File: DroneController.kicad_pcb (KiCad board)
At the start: 2 copper layers, 0.6 x 6.4 mm, 37 parts, among them P1 USB_C_Plug, U1 TP74333PDQNR, U2 TPS62152RGTR, U3 BMP280, U4 MPU-6500, U6 L86-M33, X1 X50328MSB2GI

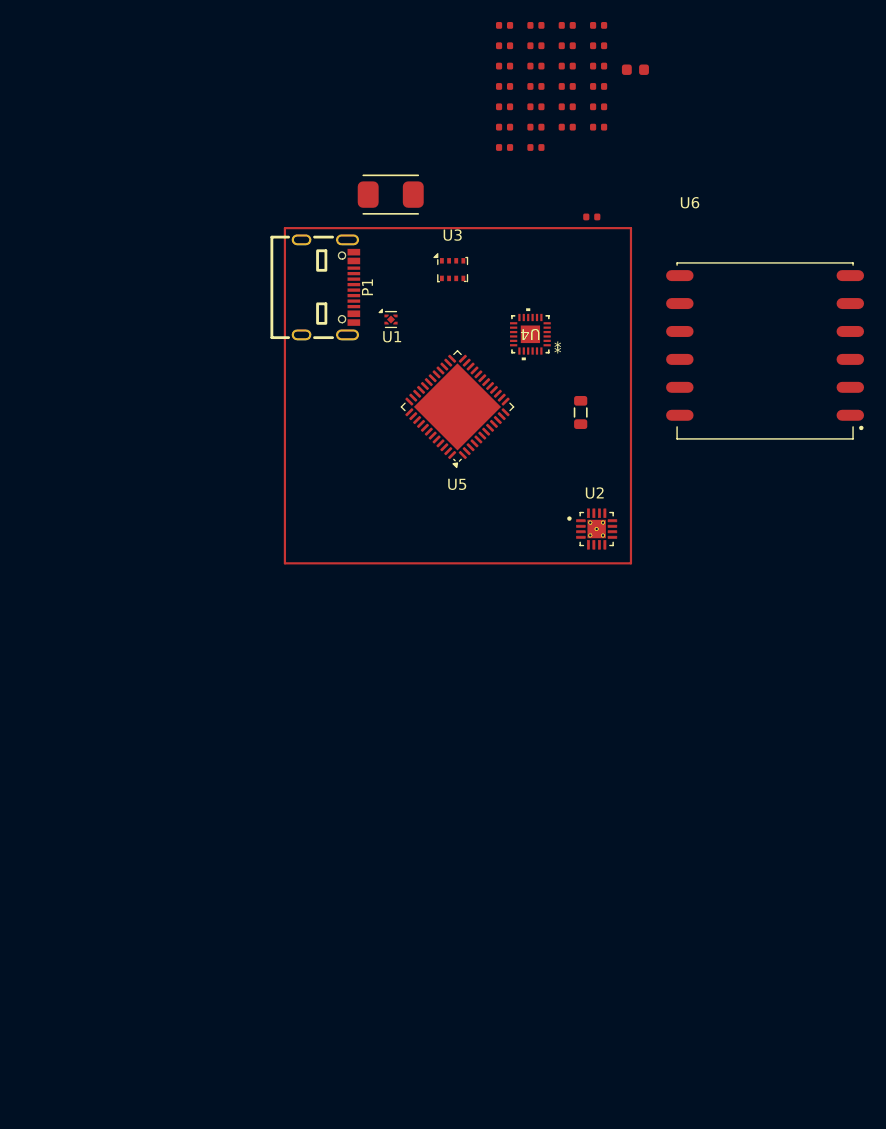
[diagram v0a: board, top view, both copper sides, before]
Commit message: Updated STM32 and overhauled SPI wiring, added external flash memory, added LoRa Transciever, moved buck converter to ESC-Board which will handle power distrubution, signficant progress on PCB design.
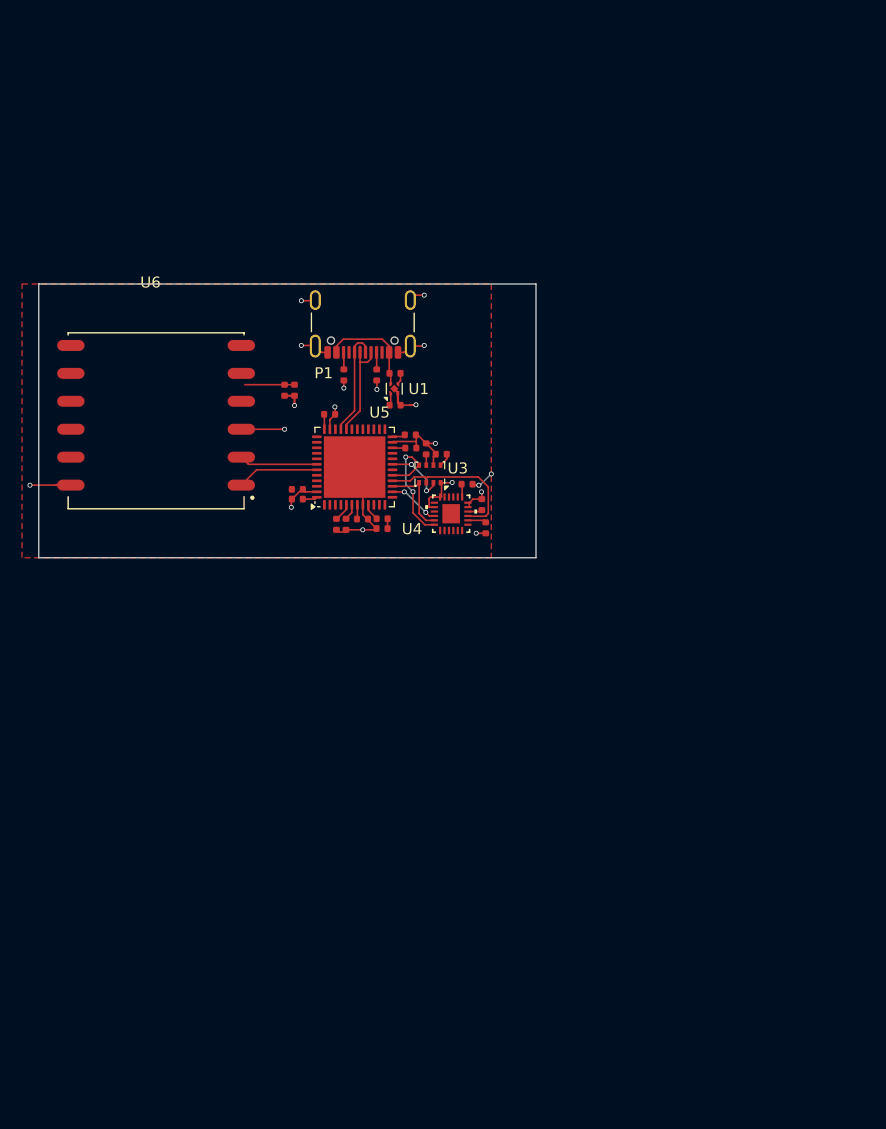
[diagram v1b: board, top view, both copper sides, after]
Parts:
- removed C11: 10uF, PCM_JLCPCB:C_0603
- removed C13: 3.3nF, PCM_JLCPCB:C_0402
- removed C19, C22, C23, C24, C8: 100nF, PCM_JLCPCB:C_0402
- removed L1: 2.2uH,50mA, PCM_JLCPCB:L_0805
- removed R3: 100kΩ, PCM_JLCPCB:R_0402
- removed U2: TPS62152RGTR, TPS62152RGTR:QFN50P300X300X100-17N
- removed X1: X50328MSB2GI, PCM_JLCPCB:CRYSTAL-SMD_L5.0-W3.2
- added C17: 100nF, PCM_JLCPCB:C_0402, F.Cu at (128.7, 101.4)
- C12: value 1uF -> 100nF
- P1: footprint MC311D:USB-C-SMD_MC-311D -> USB-C:USB-C
- moved U6 55.7 mm to (104.1, 98.3), turned to 180 degrees
- moved C10 48.9 mm to (120.5, 108.2), turned to 90 degrees
- moved C27 48.1 mm to (122.9, 107.7)
- moved C20 46.2 mm to (124.7, 107.7)
- moved C1 45.7 mm to (134.1, 108.5), turned to 90 degrees
- moved C21 45.3 mm to (124.7, 108.6), turned to 180 degrees
- moved C26 42.1 mm to (127.3, 101.3)
- moved C2 41.8 mm to (133.8, 106.4), turned to -90 degrees
- moved C7 40.6 mm to (121.4, 108.2), turned to -90 degrees
- moved C31 40.4 mm to (116.7, 96.0), turned to -90 degrees
- moved C18 38.6 mm to (117.0, 105.9), turned to 180 degrees
- moved C3 38.2 mm to (132.4, 104.6), turned to 180 degrees
- moved C12 38.1 mm to (130.1, 101.8), turned to 180 degrees
- moved C25 36.5 mm to (117.0, 105.0), turned to 180 degrees
- moved C15 34.4 mm to (115.8, 96.0), turned to -90 degrees
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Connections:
- C10 pad 1: Net-(C10-Pad1) -> GND
- C12 pad 1: Net-(C12-Pad1) -> +3.3V
- C14 pad 2: unconnected-(C14-Pad2) -> GND
- C18 pad 1: VDD -> +3.3V
- C25 pad 2: VDD -> +3.3V
- C4 pad 2: VDD -> +3.3V
- C7 pad 2: Net-(C7-Pad2) -> GND
- C9 pad 2: VDD -> +3.3V
- P1 pad B6: /USB_FS_DM -> /USB_FS_DP
- P1 pad B7: /USB_FS_DP -> /USB_FS_DM
- U3 pad 2: /SPI2_NSS -> /SPI5_NSS
- U3 pad 3: /SPI2_MOSI -> /SPI1_MISO
- U3 pad 4: /SPI2_SCK -> /SPI1_SCK
- U3 pad 5: /SPI2_MISO -> /SPI1_MOSI
- U4 pad 11: unconnected-(U4-FSYNC-Pad11) -> GND
- U4 pad 12: unconnected-(U4-INT-Pad12) -> GND
- U5 pad 1: +3.3V -> +BATT
- U5 pad 19: unconnected-(U5-PB1-Pad19) -> /SPI5_NSS
- U5 pad 24: VDD -> +3.3V
- U5 pad 25: /SPI2_NSS -> unconnected-(U5-PB12-Pad25)
- U5 pad 26: /SPI2_SCK -> unconnected-(U5-PB13-Pad26)
- U5 pad 27: /SPI2_MISO -> unconnected-(U5-PB14-Pad27)
- U5 pad 28: /SPI2_MOSI -> unconnected-(U5-PB15-Pad28)
- U5 pad 36: VDD -> +3.3V
- U5 pad 48: VDD -> +3.3V
- U5 pad 49: unconnected-(U5-PAD-Pad49) -> GND
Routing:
- net GND: track 0.00 -> 56.0 mm, vias 0 -> 17
- net /SPI1_MISO: track 0.00 -> 14.0 mm
- net /SPI1_MOSI: track 0.00 -> 12.2 mm, vias 0 -> 2
- net +3.3V: track 0.00 -> 11.3 mm, vias 0 -> 2
- net /USB_FS_DP: track 0.00 -> 9.88 mm
- net +5V: track 0.00 -> 9.35 mm
- net /USB_FS_DM: track 0.00 -> 9.21 mm
- net /USART1_RX: track 0.00 -> 7.44 mm
- net /USART1_TX: track 0.00 -> 7.13 mm
- net /SPI1_SCK: track 0.00 -> 7.13 mm
- net /SPI5_NSS: track 0.00 -> 5.76 mm, vias 0 -> 2
- net /SPI1_NSS: track 0.00 -> 4.62 mm, vias 0 -> 2
- net +BATT: track 0.00 -> 4.18 mm
- net Net-(U5-PH0-OSC_IN): track 0.00 -> 1.83 mm
- net Net-(U5-PH1-OSC_OUT): track 0.00 -> 1.67 mm
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- added copper zone on F.Cu, net +3.3V
- added copper zone on In1.Cu, net GND
- added copper zone on In2.Cu, net GND
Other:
- board size 0.6 x 6.4 mm -> 45.2 x 24.9 mm
- copper layers 2 -> 4

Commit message: Finalized PCB Design
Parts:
- removed C14, C16: 1uF, PCM_JLCPCB:C_0402
- removed C4: 4.7uF, PCM_JLCPCB:C_0402
- removed U1: TP74333PDQNR, Package_DFN_QFN:OnSemi_XDFN4-1EP_1.0x1.0mm_EP0.52x0.52mm
- added AE1: 915MHZ Antenna, Connector_Coaxial:SMA_BAT_Wireless_BWSMA-KWE-Z001, F.Cu at (147.6, 122.6)
- added C28: 100nF, PCM_JLCPCB:C_0402, F.Cu at (143.9, 115.1)
- added C29: 100nF, PCM_JLCPCB:C_0402, F.Cu at (122.0, 132.2)
- added C5: 10uF, PCM_JLCPCB:C_0402, F.Cu at (142.6, 115.1)
- added C6: 10uF, PCM_JLCPCB:C_0402, F.Cu at (107.5, 115.0)
- added C8: 10uF, PCM_JLCPCB:C_0402, F.Cu at (104.0, 115.0)
- added J1: Connector, TerminalBlock:TerminalBlock_MaiXu_MX126-5.0-02P_1x02_P5.00mm, F.Cu at (145.5, 147.1)
- added J2: Connector, TerminalBlock:TerminalBlock_MaiXu_MX126-5.0-02P_1x02_P5.00mm, F.Cu at (145.5, 135.4)
- added J3: Connector, TerminalBlock:TerminalBlock_MaiXu_MX126-5.0-02P_1x02_P5.00mm, F.Cu at (137.6, 156.0)
- added R3: 5.1kΩ, PCM_JLCPCB:R_0402, F.Cu at (137.7, 126.8)
- added R4: 5.1kΩ, PCM_JLCPCB:R_0402, F.Cu at (127.2, 128.1)
- added R5: 5.1kΩ, PCM_JLCPCB:R_0402, F.Cu at (111.1, 115.5)
- added SW1: SW_SPDT, Switches:SW-SMD_MSK12CO2, F.Cu at (135.9, 139.9)
- added U2: W25Q16JVSS, Package_SO:SOIC-8_5.3x5.3mm_P1.27mm, F.Cu at (132.5, 127.0)
- added U7: 915MHz, Lora1276:COMM-SMD_LORA1276-C1-915MHZ, F.Cu at (132.6, 115.6)
- added U9: AP7361C-33E, Package_TO_SOT_SMD:SOT-223-3_TabPin2, F.Cu at (105.9, 110.0)
- moved U6 52.3 mm to (116.5, 149.1), turned to -90 degrees
- moved P1 43.4 mm to (104.1, 128.0), turned to -90 degrees
- moved C15 41.5 mm to (113.1, 137.4), turned to 0 degrees
- moved C31 40.7 mm to (113.1, 136.5), turned to 0 degrees
- moved R2 36.9 mm to (109.8, 129.7), turned to 180 degrees
- moved C12 36.3 mm to (114.9, 134.9), turned to -90 degrees
- moved C17 36.1 mm to (116.7, 135.4), turned to 180 degrees
- moved R1 35.2 mm to (109.8, 126.8), turned to 180 degrees
- moved U3 32.3 mm to (117.0, 133.6), turned to 0 degrees
- moved C25 25.1 mm to (114.6, 130.0), turned to -90 degrees
- moved C9 24.8 mm to (116.5, 122.4), turned to -90 degrees
- moved U5 24.7 mm to (119.3, 127.5), turned to 180 degrees
- moved C3 24.5 mm to (111.9, 118.0), turned to 90 degrees
- moved C18 24.3 mm to (113.4, 130.0), turned to 90 degrees
- moved C26 23.3 mm to (117.7, 122.4), turned to 90 degrees
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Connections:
- U3 pad 2: /SPI5_NSS -> /SPI3_NSS
- U3 pad 3: /SPI1_MISO -> /SPI3_MISO
- U3 pad 4: /SPI1_SCK -> /SPI3_SCK
- U3 pad 5: /SPI1_MOSI -> /SPI3_MOSI
- U4 pad 22: /SPI1_NSS -> /SPI2_NSS
- U4 pad 23: /SPI1_SCK -> /SPI2_SCK
- U4 pad 24: /SPI1_MOSI -> /SPI2_MOSI
- U4 pad 25: unconnected-(U4-Pad25) -> GND
- U4 pad 9: /SPI1_MISO -> /SPI2_MISO
- U5 pad 12: unconnected-(U5-PA2-Pad12) -> /USART2_TX
- U5 pad 13: unconnected-(U5-PA3-Pad13) -> /USART2_RX
- U5 pad 18: unconnected-(U5-PB0-Pad18) -> /SPI5_SCK
- U5 pad 20: unconnected-(U5-PB2-Pad20) -> /Lora_RES
- U5 pad 25: unconnected-(U5-PB12-Pad25) -> /SPI2_NSS
- U5 pad 26: unconnected-(U5-PB13-Pad26) -> /SPI2_SCK
- U5 pad 27: unconnected-(U5-PB14-Pad27) -> /SPI2_MISO
- U5 pad 28: unconnected-(U5-PB15-Pad28) -> /SPI2_MOSI
- U5 pad 38: unconnected-(U5-PA15-Pad38) -> /SPI3_NSS
- U5 pad 39: unconnected-(U5-PB3-Pad39) -> /SPI3_SCK
- U5 pad 40: unconnected-(U5-PB4-Pad40) -> /SPI3_MISO
- U5 pad 41: unconnected-(U5-PB5-Pad41) -> /SPI3_MOSI
- U5 pad 44: unconnected-(U5-BOOT0-Pad44) -> Net-(SW1-B)
- U6 pad 6: unconnected-(U6-1PPS-Pad6) -> GND
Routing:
- net +3.3V: track 11.3 -> 71.6 mm, vias 2 -> 10
- net GND: track 56.0 -> 106.7 mm, vias 17 -> 57
- net /USART2_TX: track 0.00 -> 44.2 mm, vias 0 -> 2
- net /USART2_RX: track 0.00 -> 43.0 mm, vias 0 -> 2
- net +BATT: track 4.18 -> 45.2 mm, vias 0 -> 2
- net /SPI1_MOSI: track 12.2 -> 37.7 mm
- net Net-(SW1-B): track 0.00 -> 21.6 mm
- net /SPI1_SCK: track 7.13 -> 26.6 mm
- net /SPI1_MISO: track 14.0 -> 32.0 mm
- net /SPI2_MISO: track 0.00 -> 17.0 mm
- net /SPI5_NSS: track 5.76 -> 20.6 mm
- net +5V: track 9.35 -> 21.6 mm
- net /Lora_RES: track 0.00 -> 9.73 mm, vias 0 -> 2
- net /SPI2_NSS: track 0.00 -> 7.84 mm, vias 0 -> 2
- net /SPI2_MOSI: track 0.00 -> 7.67 mm, vias 0 -> 2
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- added copper zone on F.Cu, net GND
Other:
- board size 45.2 x 24.9 mm -> 50.7 x 56.1 mm
- board text added: "Flight Controller"
- board text added: "J3"

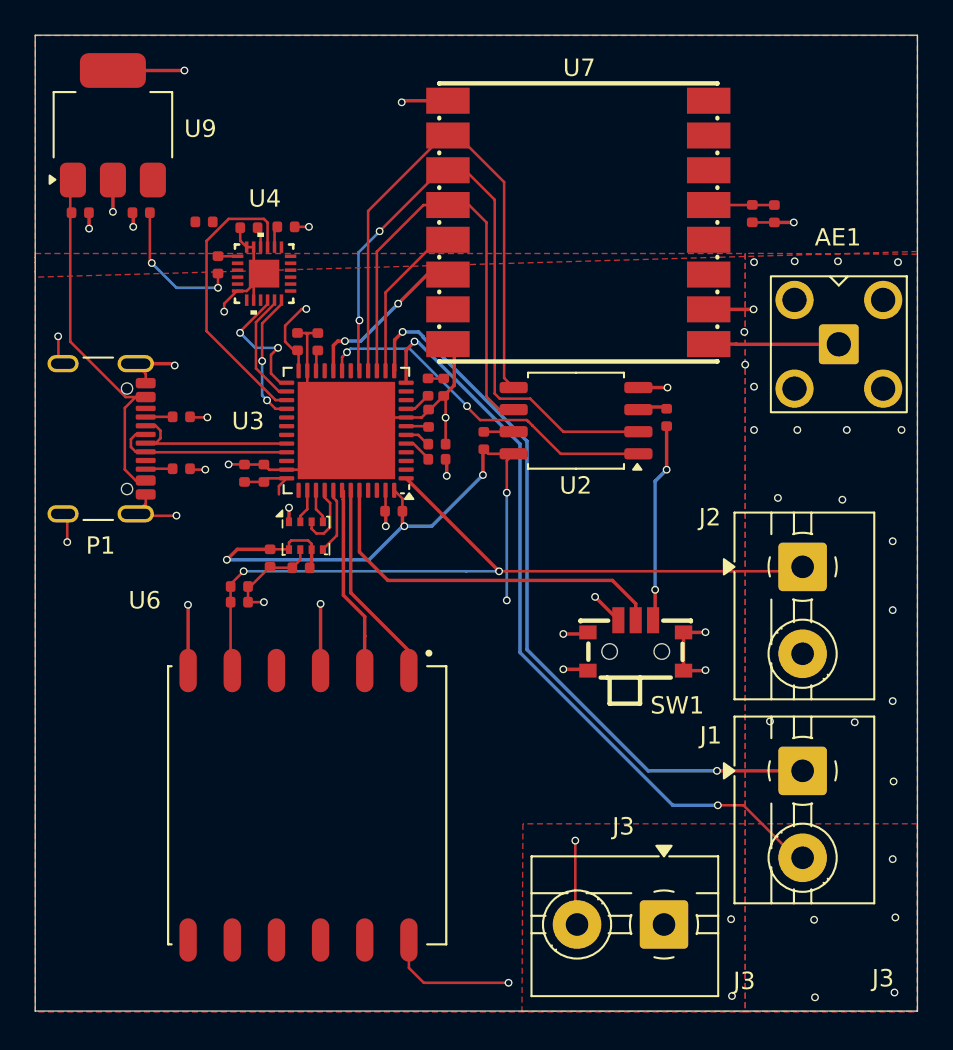
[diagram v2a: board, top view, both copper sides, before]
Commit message: Added 3D Models, Changes to Copper Zone, Added Crystal Oscillator to PCB.
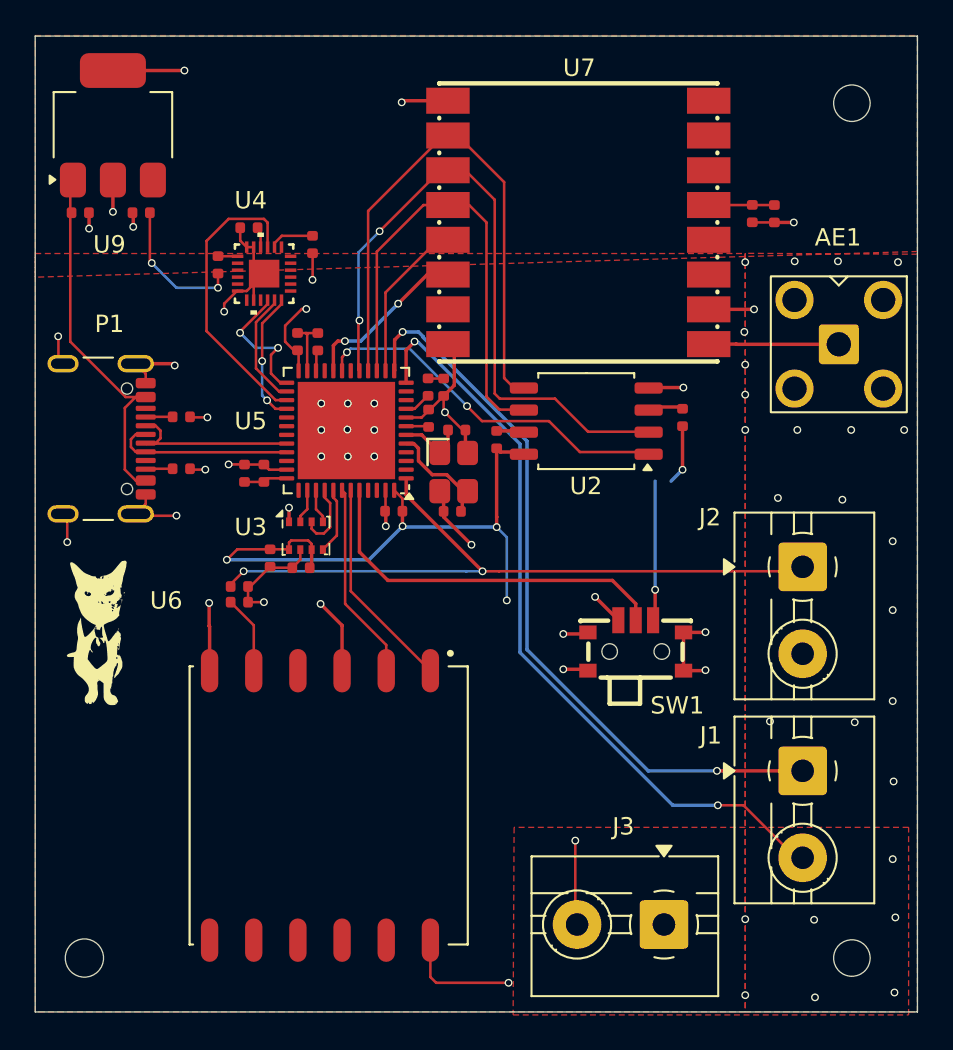
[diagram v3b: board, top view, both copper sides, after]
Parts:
- removed R5: 5.1kΩ, PCM_JLCPCB:R_0402
- added G***: LOGO, LOGO, F.Cu at (104.9, 139.2)
- added REF**: MountingHole_2.2mm_M2, MountingHole:MountingHole_2.2mm_M2, F.Cu at (104.2, 157.9)
- added REF**: MountingHole_2.1mm, MountingHole:MountingHole_2.1mm, F.Cu at (148.4, 108.7)
- added REF**: MountingHole_2.1mm, MountingHole:MountingHole_2.1mm, F.Cu at (148.4, 157.9)
- added X1: X322512MSB4SI, PCM_JLCPCB:CRYSTAL-SMD_4P-L3.2-W2.5-BL, F.Cu at (125.5, 129.9)
- moved C10 3.12 mm to (125.4, 132.2), turned to 0 degrees
- moved C1 1.83 mm to (117.3, 116.8), turned to 90 degrees
- moved C7 1.40 mm to (125.6, 127.5)
- moved U6 1.24 mm to (117.8, 149.1)
- moved R3 0.91 mm to (138.6, 126.8)
- moved R4 0.74 mm to (127.9, 128.1)
- moved U2 0.59 mm to (133.1, 127.0)
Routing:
- net GND: track 106.7 -> 98.7 mm, vias 57 -> 66
- net Net-(U5-PH0-OSC_IN): track 1.83 -> 6.41 mm
- net Net-(U5-PH1-OSC_OUT): track 1.67 -> 3.88 mm
- net +3.3V: track 71.6 -> 70.0 mm, vias 10 -> 9
- net /SPI5_NSS: track 20.6 -> 21.1 mm
- net /USART1_RX: track 11.8 -> 12.3 mm
- net /USART1_TX: track 10.9 -> 11.4 mm
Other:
- board text added: "U4"
- board text added: "U5"
- board text removed: "J3"

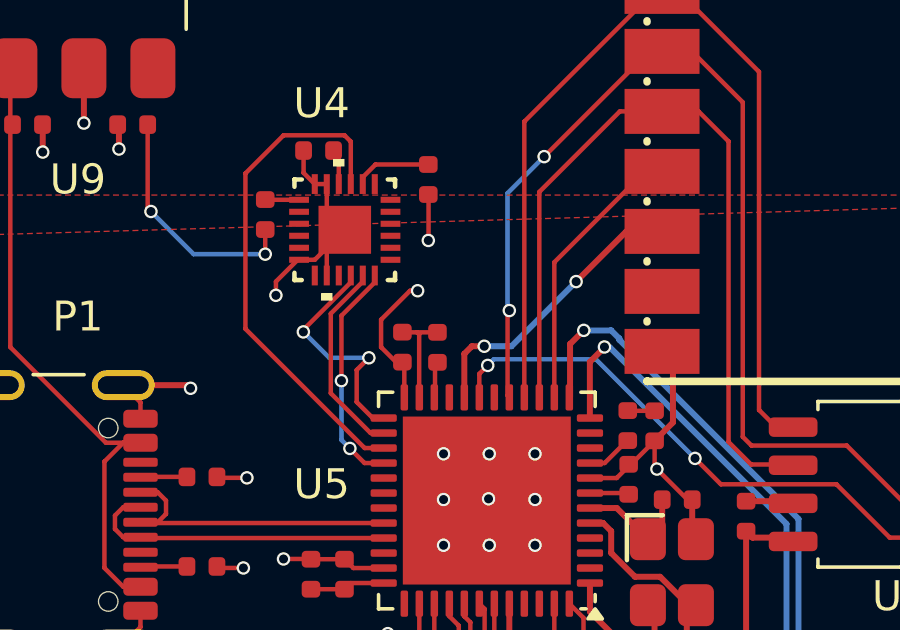
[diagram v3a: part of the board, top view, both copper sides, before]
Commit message: added mounting holes
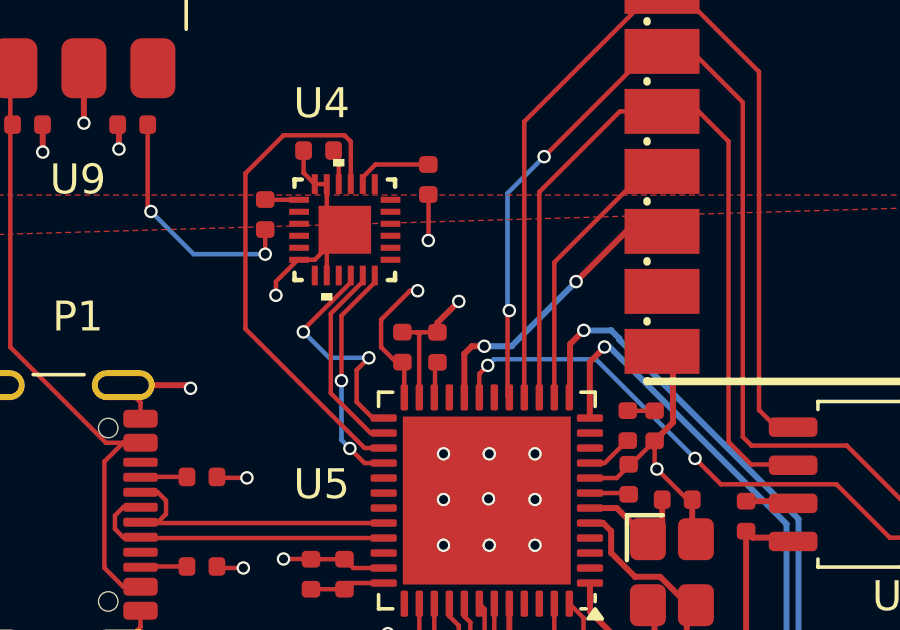
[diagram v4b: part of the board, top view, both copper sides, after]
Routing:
- net GND: track 98.7 -> 100.1 mm, vias 66 -> 67
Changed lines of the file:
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@@
+	)
+	(segment
+		(start 117.6528 121.6152)
+		(end 118.364 120.904)
+		(width 0.2)
+		(layer "F.Cu")
+		(net 59)
 	)
 	(segment
@@
 	)
 	(segment
+		(start 117.6528 121.934704)
+		(end 117.6528 121.6152)
+		(width 0.2)
+		(layer "F.Cu")
+		(net 59)
+	)
+	(segment
 		(start 133.1124 141.2748)
 		(end 133.1908 141.3532)
@@
 		(net 59)
 	)
+	(via
+		(at 118.364 120.904)
+		(size 0.45)
+		(drill 0.3)
+		(layers "F.Cu" "B.Cu")
+		(net 59)
+	)

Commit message: Added LCSC Part Numbers
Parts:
- added D1: PMEG3015EJ, Diode_SMD:D_SOD-323F, F.Cu at (137.6, 149.7)
- added D2: PMEG3015EJ, Diode_SMD:D_SOD-323F, F.Cu at (109.5, 116.1)
- moved G*** 2.04 mm to (104.3, 141.1)
- moved U6 0.36 mm to (117.4, 149.2)
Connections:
- net /USB_FS_DM renamed /USB_FS_DN
- C6 pad 1: +3.3V -> Net-(D2-A)
- J3 pad 1: +3.3V -> /LIPO_3.3V
- U9 pad 3: +3.3V -> Net-(D2-A)
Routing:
- net /LIPO_3.3V: track 0.00 -> 5.14 mm
- net Net-(D2-A): track 0.00 -> 3.49 mm
- net +3.3V: track 70.0 -> 66.8 mm
- net /USB_FS_DN: track 10.6 -> 8.75 mm
- net /USB_FS_DP: track 10.5 -> 11.2 mm
- net GND: track 100.1 -> 100.7 mm
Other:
- board text added: "This is the MK I of the AmmarAndEvan Flight Computer. This is a joint interdisciplinary project in which we build a FPV Drone. More iterations will follow."
